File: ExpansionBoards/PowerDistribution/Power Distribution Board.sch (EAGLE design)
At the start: 23 parts, among them J1 350211-1, J10 640445-3, J11 640445-5, J12 640445-8, J13 640445-6, J2 216571-2005, J3 216571-2004, J4 216571-2003, J5 350211-1, J6 216571-2002, J7 216571-2008, J8 640445-4, J9 640445-2, K1 AHQSS105DM2FA0G, U3 LM338T/NOPB

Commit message: expansion board improvements
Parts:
- added J14: 216571-2003, SamacSys_Parts:216571-2003
- J8: value 640445-4 -> 640445-6; device SamacSys_Parts:640445-4 -> SamacSys_Parts:640445-6
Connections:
- net 12V: now also J8.5; no longer J8.4
- net 5V: now also J8.6; no longer J8.1
- net GND: now also J14.2, J8.1, J8.4
- net LINE_HOT_IN: now also J14.3
- net LINE_NEUTRAL: now also J14.1
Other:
- note added: "120VAC MAINS INPUT"
- note added: "SECONDARY PSU SWITCHING RELAY Connects 120VAC mains line-in power to the secondary supplies when PC is on."
- note removed: "SECONDARY PSU SWITCHING RELAY Switches power to the secondary supplies when PC is on."
- moved on the sheet: J1, K1

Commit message: Add ButtonLatencyTester2
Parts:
- removed C31: 0.1uF, rcl:C-USC1206
- removed R29: 270R, rcl:R-US_R1206
- removed R30: 1.1K, rcl:R-US_R1206
- added C5: SLPX682M080H7P3, SamacSys_Parts:SLPX682M080H7P3
- added J15: 640445-6, SamacSys_Parts:640445-6
- added LED1: (no value), led:LED5MM
- added R1: 2.4K/1W, rcl:R-US_0309/12
- added R2: 1.1K, rcl:R-US_0204/7
- added R3: 270R, rcl:R-US_0204/7
- C1: device rcl:CPOL-US_TANTALUMC1206 -> rcl:CPOL-US_TANTALUMB45181A
- C2: value SLPX682M080H7P3 -> 0.1uF; device SamacSys_Parts:SLPX682M080H7P3 -> rcl:C-US025-030X050
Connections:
- new net N$3: LED1.A, R1.1
- net 12V: now also C2.1, J15.5; no longer C31.1
- net 48V: now also C5.+, R1.2; no longer C2.+
- net 5V: now also J15.6
- net 6V3: now also R3.2; no longer R29.2
- net GND: now also C2.2, C5.-, J15.1, J15.2, J15.3, J15.4, LED1.C, R2.1; no longer C2.-, C31.2, R30.1
- net N$32: now also R2.2, R3.1; no longer R29.1, R30.2
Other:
- note added: "Generic 5mm LED Vf approx 2V, If 20mA Indicator + drains caps when power is off"
- note added: "To Pinscape Pico Main Board Secondary PSU Power Input"
- note added: "To Pinscape Pico Power Board Secondary PSU Power Input"
- note removed: "To Pinscape Pico Board Secondary PSU Power Input"

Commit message: KL25Z adapter board updates;
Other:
- moved on the sheet: C3, C4, C5, J2, J3, J5, J6, J7, LED1, R1, RT1

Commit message: PCB parts lists (BOMs); power distro board edits
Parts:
- removed J6: 216571-2002, SamacSys_Parts:216571-2002
- added J16: 640445-8, SamacSys_Parts:640445-8
- C1: device rcl:CPOL-US_TANTALUMB45181A -> rcl:CPOL-US_TANTALUMB45181B
- J1: value 350211-1 -> 216571-2002; device SamacSys_Parts:350211-1 -> SamacSys_Parts:216571-2002
- J10: value 640445-3 -> 640445-6; device SamacSys_Parts:640445-3 -> SamacSys_Parts:640445-6
- J11: value 640445-5 -> 640445-6; device SamacSys_Parts:640445-5 -> SamacSys_Parts:640445-6
- J12: value 640445-8 -> 640445-2; device SamacSys_Parts:640445-8 -> SamacSys_Parts:640445-2
- J13: value 640445-6 -> 640445-5; device SamacSys_Parts:640445-6 -> SamacSys_Parts:640445-5
- J14: value 216571-2003 -> 640445-3; device SamacSys_Parts:216571-2003 -> SamacSys_Parts:640445-3
- J15: value 640445-6 -> 216571-2003; device SamacSys_Parts:640445-6 -> SamacSys_Parts:216571-2003
- J3: value 216571-2004 -> 216571-2005; device SamacSys_Parts:216571-2004 -> SamacSys_Parts:216571-2005
- J4: value 216571-2003 -> 350211-1; device SamacSys_Parts:216571-2003 -> SamacSys_Parts:350211-1
- J5: value 350211-1 -> 206832-1001; device SamacSys_Parts:350211-1 -> SamacSys_Parts:206832-1001
- J7: value 216571-2008 -> 216571-2003; device SamacSys_Parts:216571-2008 -> SamacSys_Parts:216571-2003
- J8: value 640445-6 -> 350211-1; device SamacSys_Parts:640445-6 -> SamacSys_Parts:350211-1
- J9: value 640445-2 -> 640445-6; device SamacSys_Parts:640445-2 -> SamacSys_Parts:640445-6
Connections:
- net 12V: now also J10.5, J13.1, J13.2, J13.3, J13.4, J13.5, J4.1, J5.2, J9.5; no longer J11.1, J11.2, J11.3, J11.4, J11.5, J15.5, J5.1, J7.3, J8.5
- net 12VPC: now also J8.1; no longer J1.1
- net 24V: now also J14.1, J14.2, J14.3, J3.2; no longer J10.1, J10.2, J10.3, J2.3
- net 48V: now also J15.1, J15.2, J15.3; no longer J4.1, J4.2, J4.3
- net 5V: now also J10.6, J11.1, J11.2, J11.3, J11.4, J11.5, J11.6, J4.4, J5.7, J9.6; no longer J13.1, J13.2, J13.3, J13.4, J13.5, J13.6, J15.6, J5.4, J7.6, J8.6
- net 5VPC: now also J8.4; no longer J1.4
- net 6V3: now also J12.1, J12.2; no longer J9.1, J9.2
- net GND: now also J10.1, J10.2, J10.3, J10.4, J16.1, J16.2, J16.3, J16.4, J16.5, J16.6, J16.7, J16.8, J2.3, J3.3, J4.2, J4.3, J5.1, J5.6, J5.8, J9.1, J9.2, J9.3, J9.4; no longer J1.2, J1.3, J12.1, J12.2, J12.3, J12.4, J12.5, J12.6, J12.7, J12.8, J14.2, J15.1, J15.2, J15.3, J15.4, J2.2, J5.2, J7.1, J8.1, J8.4
- net LINE_HOT: now also J3.5, J5.10, J5.5; no longer J3.4, J7.5, J7.8
- net LINE_HOT_IN: now also J7.3; no longer J14.3
- net LINE_NEUTRAL: now also J3.4, J5.4, J5.9, J7.1; no longer J14.1, J3.3, J7.4, J7.7
- net N$1: now also J1.2, J2.2; no longer J3.2, J6.2
- net N$2: now also J1.1; no longer J6.1
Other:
- note added: "Generic 5mm LED Vf approx 3.2V, If 20mA Indicator + drains caps when power is off"
- note removed: "Generic 5mm LED Vf approx 2V, If 20mA Indicator + drains caps when power is off"

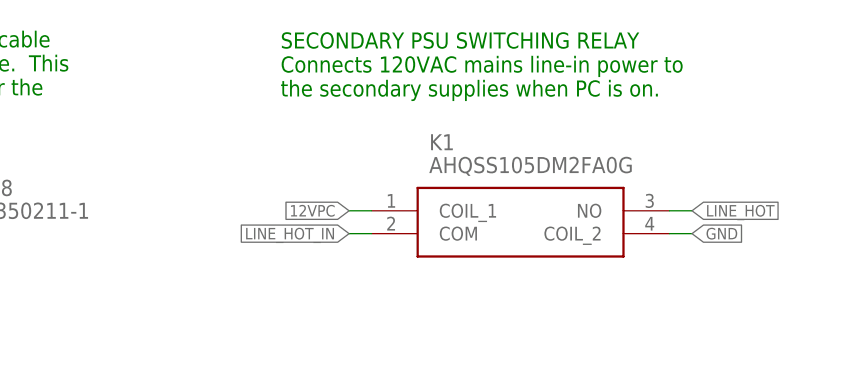
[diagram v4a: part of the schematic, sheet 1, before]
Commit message: exp board: power distro: add relay coil diode
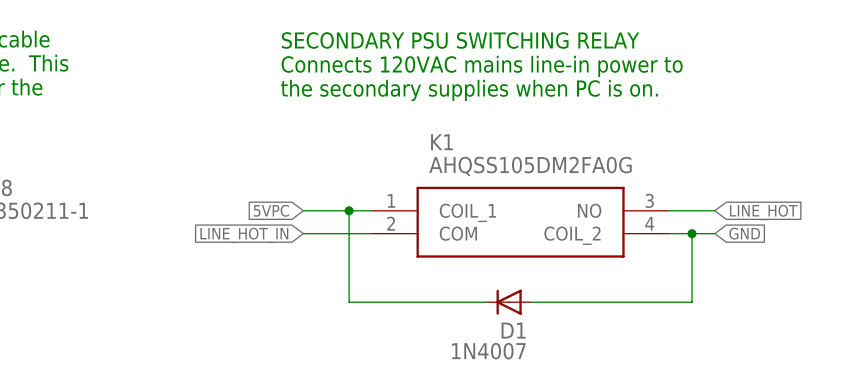
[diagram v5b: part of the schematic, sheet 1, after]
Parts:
- added D1: 1N4007, diode:1N4007
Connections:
- net 12VPC: no longer K1.COIL_1
- net 5VPC: now also D1.C, K1.COIL_1
- net GND: now also D1.A
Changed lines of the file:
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@@
 <grid distance="0.1" unitdist="inch" unit="inch" style="lines" multiple="1" display="no" altdistance="0.01" altunitdist="inch" altunit="inch"/>
 <layers>
-<layer number="1" name="Top" color="4" fill="1" visible="yes" active="no"/>
-<layer number="2" name="Route2" color="1" fill="3" visible="yes" active="no"/>
-<layer number="3" name="Route3" color="4" fill="3" visible="yes" active="no"/>
-<layer number="14" name="Route14" color="1" fill="6" visible="yes" active="no"/>
-<layer number="15" name="Route15" color="4" fill="6" visible="yes" active="no"/>
-<layer number="16" name="Bottom" color="1" fill="1" visible="yes" active="no"/>
-<layer number="17" name="Pads" color="2" fill="1" visible="yes" active="no"/>
-<layer number="18" name="Vias" color="2" fill="1" visible="yes" active="no"/>
-<layer number="19" name="Unrouted" color="6" fill="1" visible="yes" active="no"/>
-<layer number="20" name="Dimension" color="15" fill="1" visible="yes" active="no"/>
-<layer number="21" name="tPlace" color="7" fill="1" visible="yes" active="no"/>
-<layer number="22" name="bPlace" color="7" fill="1" visible="yes" active="no"/>
-<layer number="23" name="tOrigins" color="15" fill="1" visible="yes" active="no"/>
-<layer number="24" name="bOrigins" color="15" fill="1" visible="yes" active="no"/>
-<layer number="25" name="tNames" color="7" fill="1" visible="yes" active="no"/>
-<layer number="26" name="bNames" color="7" fill="1" visible="yes" active="no"/>
-<layer number="27" name="tValues" color="7" fill="1" visible="yes" active="no"/>
-<layer number="28" name="bValues" color="7" fill="1" visible="yes" active="no"/>
+<layer number="1" name="Top" color="4" fill="1" visible="no" active="no"/>
+<layer number="2" name="Route2" color="1" fill="3" visible="no" active="no"/>
+<layer number="3" name="Route3" color="4" fill="3" visible="no" active="no"/>
+<layer number="14" name="Route14" color="1" fill="6" visible="no" active="no"/>
+<layer number="15" name="Route15" color="4" fill="6" visible="no" active="no"/>
+<layer number="16" name="Bottom" color="1" fill="1" visible="no" active="no"/>
+<layer number="17" name="Pads" color="2" fill="1" visible="no" active="no"/>
+<layer number="18" name="Vias" color="2" fill="1" visible="no" active="no"/>
+<layer number="19" name="Unrouted" color="6" fill="1" visible="no" active="no"/>
+<layer number="20" name="Dimension" color="15" fill="1" visible="no" active="no"/>
+<layer number="21" name="tPlace" color="7" fill="1" visible="no" active="no"/>
+<layer number="22" name="bPlace" color="7" fill="1" visible="no" active="no"/>
+<layer number="23" name="tOrigins" color="15" fill="1" visible="no" active="no"/>
+<layer number="24" name="bOrigins" color="15" fill="1" visible="no" active="no"/>
+<layer number="25" name="tNames" color="7" fill="1" visible="no" active="no"/>
+<layer number="26" name="bNames" color="7" fill="1" visible="no" active="no"/>
+<layer number="27" name="tValues" color="7" fill="1" visible="no" active="no"/>
+<layer number="28" name="bValues" color="7" fill="1" visible="no" active="no"/>
 <layer number="29" name="tStop" color="7" fill="3" visible="no" active="no"/>
 <layer number="30" name="bStop" color="7" fill="6" visible="no" active="no"/>
@@
 <layer number="35" name="tGlue" color="7" fill="4" visible="no" active="no"/>
 <layer number="36" name="bGlue" color="7" fill="5" visible="no" active="no"/>
-<layer number="37" name="tTest" color="7" fill="1" visible="yes" active="no"/>
-<layer number="38" name="bTest" color="7" fill="1" visible="yes" active="no"/>
+<layer number="37" name="tTest" color="7" fill="1" visible="no" active="no"/>
+<layer number="38" name="bTest" color="7" fill="1" visible="no" active="no"/>
 <layer number="39" name="tKeepout" color="4" fill="11" visible="no" active="no"/>
 <layer number="40" name="bKeepout" color="1" fill="11" visible="no" active="no"/>
@@
 <layer number="44" name="Drills" color="7" fill="1" visible="no" active="no"/>
 <layer number="45" name="Holes" color="7" fill="1" visible="no" active="no"/>
-<layer number="46" name="Milling" color="3" fill="1" visible="yes" active="no"/>
-<layer number="47" name="Measures" color="7" fill="1" visible="yes" active="no"/>
-<layer number="48" name="Document" color="7" fill="1" visible="yes" active="no"/>
-<layer number="49" name="Reference" color="7" fill="1" visible="yes" active="no"/>
-<layer number="50" name="dxf" color="7" fill="1" visible="yes" active="no"/>
-<layer number="51" name="tDocu" color="7" fill="1" visible="yes" active="no"/>
-<layer number="52" name="bDocu" color="7" fill="1" visible="yes" active="no"/>
-<layer number="53" name="tPadExt" color="7" fill="1" visible="yes" active="no"/>
-<layer number="54" name="bPadExt" color="1" fill="1" visible="yes" active="no"/>
+<layer number="46" name="Milling" color="3" fill="1" visible="no" active="no"/>
+<layer number="47" name="Measures" color="7" fill="1" visible="no" active="no"/>
+<layer number="48" name="Document" color="7" fill="1" visible="no" active="no"/>
+<layer number="49" name="Reference" color="7" fill="1" visible="no" active="no"/>
+<layer number="50" name="dxf" color="7" fill="1" visible="no" active="no"/>
+<layer number="51" name="tDocu" color="7" fill="1" visible="no" active="no"/>
+<layer number="52" name="bDocu" color="7" fill="1" visible="no" active="no"/>
+<layer number="53" name="tPadExt" color="7" fill="1" visible="no" active="no"/>
+<layer number="54" name="bPadExt" color="1" fill="1" visible="no" active="no"/>
 <layer number="88" name="SimResults" color="9" fill="1" visible="yes" active="yes"/>
 <layer number="89" name="SimProbes" color="9" fill="1" visible="yes" active="yes"/>
@@
 <part name="R1" library="rcl" deviceset="R-US_" device="0309/12" value="2.4K/1W"/>
 <part name="J5" library="SamacSys_Parts" deviceset="206832-1001" device=""/>
+<part name="D1" library="diode" deviceset="1N4007" device=""/>
 </parts>
 <sheets>
@@
 <attribute name="VALUE" x="39.37" y="50.8" size="1.778" layer="96" align="center-left"/>
 </instance>
+<instance part="D1" gate="1" x="96.52" y="0" smashed="yes" rot="R180">
+<attribute name="NAME" x="98.552" y="-2.2606" size="1.778" layer="95" rot="R180"/>
+<attribute name="VALUE" x="98.552" y="-4.5466" size="1.778" layer="96" rot="R180"/>
+</instance>
 </instances>
 <busses>
@@
 <segment>
 <pinref part="K1" gate="G$1" pin="COIL_2"/>
+<wire x1="119.38" y1="7.62" x2="116.84" y2="7.62" width="0.1524" layer="91"/>
+<label x="119.38" y="7.62" size="1.27" layer="95" xref="yes"/>
+<pinref part="D1" gate="1" pin="A"/>
 <wire x1="116.84" y1="7.62" x2="114.3" y2="7.62" width="0.1524" layer="91"/>
-<label x="116.84" y="7.62" size="1.27" layer="95" xref="yes"/>
+<wire x1="99.06" y1="0" x2="116.84" y2="0" width="0.1524" layer="91"/>
+<wire x1="116.84" y1="0" x2="116.84" y2="7.62" width="0.1524" layer="91"/>
+<junction x="116.84" y="7.62"/>
 </segment>
 <segment>
@@
 <label x="20.32" y="12.7" size="1.27" layer="95" rot="R180" xref="yes"/>
 </segment>
+<segment>
+<pinref part="K1" gate="G$1" pin="COIL_1"/>
+<wire x1="73.66" y1="10.16" x2="78.74" y2="10.16" width="0.1524" layer="91"/>
+<label x="73.66" y="10.16" size="1.27" layer="95" rot="R180" xref="yes"/>
+<wire x1="78.74" y1="10.16" x2="81.28" y2="10.16" width="0.1524" layer="91"/>
+<wire x1="78.74" y1="10.16" x2="78.74" y2="0" width="0.1524" layer="91"/>
+<junction x="78.74" y="10.16"/>
+<pinref part="D1" gate="1" pin="C"/>
+<wire x1="78.74" y1="0" x2="93.98" y2="0" width="0.1524" layer="91"/>
+</segment>
 </net>
 <net name="12VPC" class="0">
@@
 <label x="20.32" y="5.08" size="1.27" layer="95" rot="R180" xref="yes"/>
 </segment>
-<segment>
-<pinref part="K1" gate="G$1" pin="COIL_1"/>
-<wire x1="78.74" y1="10.16" x2="81.28" y2="10.16" width="0.1524" layer="91"/>
-<label x="78.74" y="10.16" size="1.27" layer="95" rot="R180" xref="yes"/>
-</segment>
 </net>
 <net name="LINE_HOT" class="0">
 <segment>
 <pinref part="K1" gate="G$1" pin="NO"/>
-<wire x1="116.84" y1="10.16" x2="114.3" y2="10.16" width="0.1524" layer="91"/>
-<label x="116.84" y="10.16" size="1.27" layer="95" xref="yes"/>
+<wire x1="119.38" y1="10.16" x2="114.3" y2="10.16" width="0.1524" layer="91"/>
+<label x="119.38" y="10.16" size="1.27" layer="95" xref="yes"/>
 </segment>
 </net>
@@
 <segment>
 <pinref part="K1" gate="G$1" pin="COM"/>
-<wire x1="78.74" y1="7.62" x2="81.28" y2="7.62" width="0.1524" layer="91"/>
-<label x="78.74" y="7.62" size="1.27" layer="95" rot="R180" xref="yes"/>
-</segment>
-<segment>
+<wire x1="73.66" y1="7.62" x2="81.28" y2="7.62" width="0.1524" layer="91"/>
+<label x="73.66" y="7.62" size="1.27" layer="95" rot="R180" xref="yes"/>
+</segment>
+<segment>

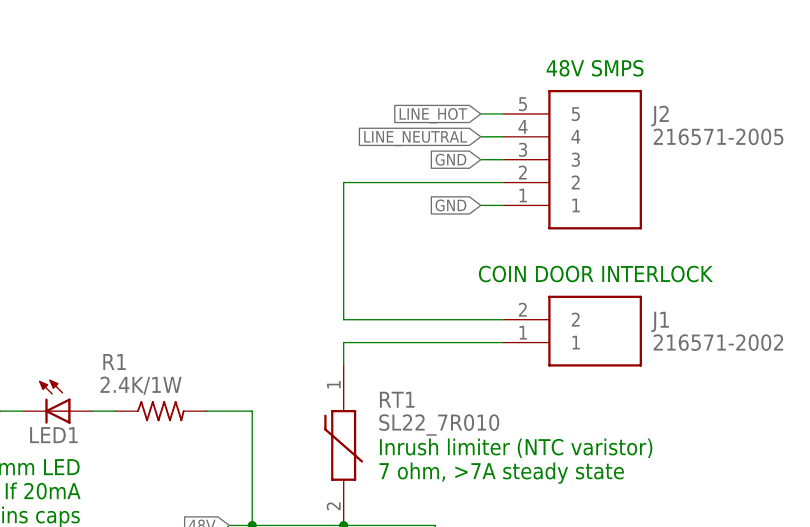
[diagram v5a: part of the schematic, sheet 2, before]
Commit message: exp board: power distro: change coin door interlock to AC
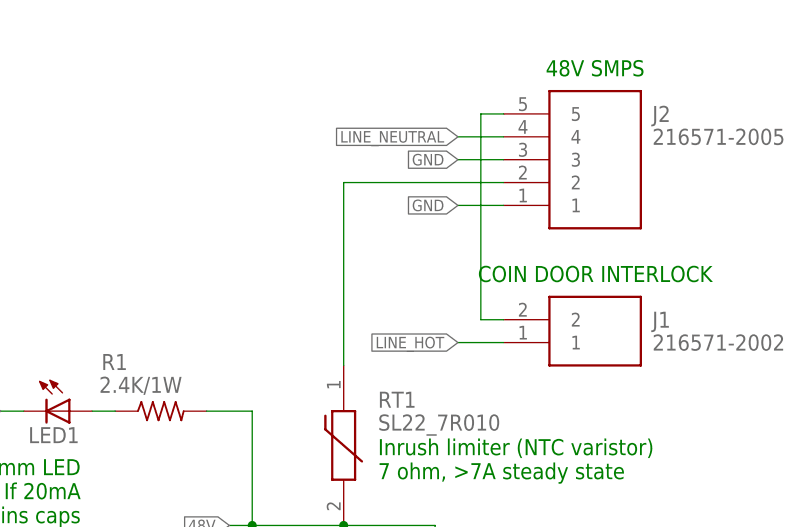
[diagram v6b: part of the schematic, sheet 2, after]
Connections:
- removed net N$2: J1.1, RT1.1
- new net N$4: J1.2, J2.5
- net LINE_HOT: now also J1.1; no longer J2.5
- net N$1: now also RT1.1; no longer J1.2
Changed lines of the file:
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@@
 </segment>
 <segment>
-<label x="162.56" y="76.2" size="1.27" layer="95" rot="R180" xref="yes"/>
-<pinref part="J2" gate="G$1" pin="5"/>
-<wire x1="165.1" y1="76.2" x2="162.56" y2="76.2" width="0.1524" layer="91"/>
+<label x="160.02" y="50.8" size="1.27" layer="95" rot="R180" xref="yes"/>
+<pinref part="J1" gate="G$1" pin="1"/>
+<wire x1="160.02" y1="50.8" x2="165.1" y2="50.8" width="0.1524" layer="91"/>
 </segment>
 <segment>
@@
 </segment>
 <segment>
-<label x="162.56" y="73.66" size="1.27" layer="95" rot="R180" xref="yes"/>
+<label x="160.02" y="73.66" size="1.27" layer="95" rot="R180" xref="yes"/>
 <pinref part="J2" gate="G$1" pin="4"/>
-<wire x1="165.1" y1="73.66" x2="162.56" y2="73.66" width="0.1524" layer="91"/>
+<wire x1="165.1" y1="73.66" x2="160.02" y2="73.66" width="0.1524" layer="91"/>
 </segment>
 <segment>
@@
 <segment>
 <pinref part="J2" gate="G$1" pin="1"/>
-<wire x1="162.56" y1="66.04" x2="165.1" y2="66.04" width="0.1524" layer="91"/>
-<label x="162.56" y="66.04" size="1.27" layer="95" rot="R180" xref="yes"/>
+<wire x1="160.02" y1="66.04" x2="165.1" y2="66.04" width="0.1524" layer="91"/>
+<label x="160.02" y="66.04" size="1.27" layer="95" rot="R180" xref="yes"/>
 </segment>
 <segment>
@@
 </segment>
 <segment>
-<label x="162.56" y="71.12" size="1.27" layer="95" rot="R180" xref="yes"/>
+<label x="160.02" y="71.12" size="1.27" layer="95" rot="R180" xref="yes"/>
 <pinref part="J2" gate="G$1" pin="3"/>
-<wire x1="162.56" y1="71.12" x2="165.1" y2="71.12" width="0.1524" layer="91"/>
+<wire x1="160.02" y1="71.12" x2="165.1" y2="71.12" width="0.1524" layer="91"/>
 </segment>
 <segment>
@@
 <pinref part="J2" gate="G$1" pin="2"/>
 <wire x1="165.1" y1="68.58" x2="147.32" y2="68.58" width="0.1524" layer="91"/>
-<wire x1="147.32" y1="68.58" x2="147.32" y2="53.34" width="0.1524" layer="91"/>
-<pinref part="J1" gate="G$1" pin="2"/>
-<wire x1="147.32" y1="53.34" x2="165.1" y2="53.34" width="0.1524" layer="91"/>
-</segment>
-</net>
-<net name="N$2" class="0">
-<segment>
-<pinref part="J1" gate="G$1" pin="1"/>
-<wire x1="165.1" y1="50.8" x2="147.32" y2="50.8" width="0.1524" layer="91"/>
+<wire x1="147.32" y1="68.58" x2="147.32" y2="48.26" width="0.1524" layer="91"/>
 <pinref part="RT1" gate="G$1" pin="1"/>
-<wire x1="147.32" y1="50.8" x2="147.32" y2="48.26" width="0.1524" layer="91"/>
 </segment>
 </net>
@@
 </segment>
 </net>
+<net name="N$4" class="0">
+<segment>
+<pinref part="J2" gate="G$1" pin="5"/>
+<wire x1="165.1" y1="76.2" x2="162.56" y2="76.2" width="0.1524" layer="91"/>
+<wire x1="162.56" y1="76.2" x2="162.56" y2="53.34" width="0.1524" layer="91"/>
+<pinref part="J1" gate="G$1" pin="2"/>
+<wire x1="162.56" y1="53.34" x2="165.1" y2="53.34" width="0.1524" layer="91"/>
+</segment>
+</net>
